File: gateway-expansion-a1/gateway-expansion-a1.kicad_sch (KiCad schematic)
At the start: 3 parts, among them J1 Ruuvi Connector, J2 Ruuvi Connector, J3 Ruuvi Connector

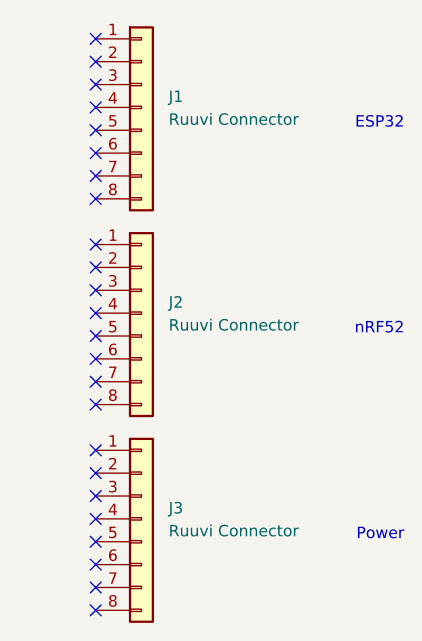
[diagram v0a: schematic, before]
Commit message: Add copper zones and export gerbers
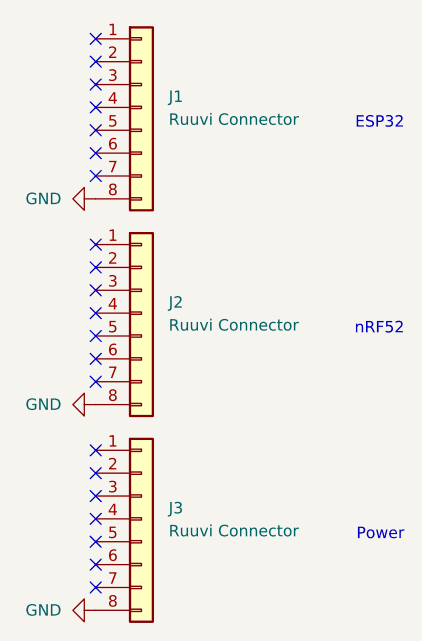
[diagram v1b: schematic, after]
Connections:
- net GND: now reaches J2.8 (Pin_8)
- net GND: now also J1.8 (Pin_8), J3.8 (Pin_8)
- no-connect marks 24 -> 21
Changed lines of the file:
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@@
     (rev "A1")
   )
+  (no_connect (at 124.46 99.06))
+  (no_connect (at 124.46 109.22))
+  (no_connect (at 124.46 129.54))
+  (no_connect (at 124.46 76.2))
+  (no_connect (at 124.46 86.36))
+  (no_connect (at 124.46 83.82))
+  (no_connect (at 124.46 104.14))
+  (no_connect (at 124.46 106.68))
   (no_connect (at 124.46 119.38))
+  (no_connect (at 124.46 127))
+  (no_connect (at 124.46 121.92))
+  (no_connect (at 124.46 81.28))
+  (no_connect (at 124.46 78.74))
+  (no_connect (at 124.46 73.66))
+  (no_connect (at 124.46 132.08))
+  (no_connect (at 124.46 93.98))
   (no_connect (at 124.46 124.46))
-  (no_connect (at 124.46 86.36))
-  (no_connect (at 124.46 81.28))
-  (no_connect (at 124.46 76.2))
-  (no_connect (at 124.46 111.76))
-  (no_connect (at 124.46 104.14))
-  (no_connect (at 124.46 88.9))
-  (no_connect (at 124.46 129.54))
+  (no_connect (at 124.46 116.84))
+  (no_connect (at 124.46 71.12))
+  (no_connect (at 124.46 101.6))
   (no_connect (at 124.46 96.52))
-  (no_connect (at 124.46 116.84))
-  (no_connect (at 124.46 83.82))
-  (no_connect (at 124.46 121.92))
-  (no_connect (at 124.46 109.22))
-  (no_connect (at 124.46 71.12))
-  (no_connect (at 124.46 134.62))
-  (no_connect (at 124.46 93.98))
-  (no_connect (at 124.46 73.66))
-  (no_connect (at 124.46 127))
-  (no_connect (at 124.46 132.08))
-  (no_connect (at 124.46 99.06))
-  (no_connect (at 124.46 101.6))
-  (no_connect (at 124.46 78.74))
-  (no_connect (at 124.46 106.68))
   (text "ESP32" (at 158.75 81.28 180)
     (effects (font (size 1.27 1.27)) (justify right bottom))
@@
   (text "Power" (at 158.75 127 180)
     (effects (font (size 1.27 1.27)) (justify right bottom))
+  )
+  (symbol (lib_id "power:GND") (at 124.46 88.9 270) (unit 1)
+    (in_bom yes) (on_board yes)
+    (property "Reference" "#PWR?" (id 0) (at 118.11 88.9 0)
+      (effects (font (size 1.27 1.27)) hide)
+    )
+    (property "Value" "GND" (id 1) (at 120.65 88.9 90)
+      (effects (font (size 1.27 1.27)) (justify right))
+    )
+    (property "Footprint" "" (id 2) (at 124.46 88.9 0)
+      (effects (font (size 1.27 1.27)) hide)
+    )
+    (property "Datasheet" "" (id 3) (at 124.46 88.9 0)
+      (effects (font (size 1.27 1.27)) hide)
+    )
+  )
+  (symbol (lib_id "power:GND") (at 124.46 111.76 270) (unit 1)
+    (in_bom yes) (on_board yes)
+    (property "Reference" "#PWR?" (id 0) (at 118.11 111.76 0)
+      (effects (font (size 1.27 1.27)) hide)
+    )
+    (property "Value" "GND" (id 1) (at 120.65 111.76 90)
+      (effects (font (size 1.27 1.27)) (justify right))
+    )
+    (property "Footprint" "" (id 2) (at 124.46 111.76 0)
+      (effects (font (size 1.27 1.27)) hide)
+    )
+    (property "Datasheet" "" (id 3) (at 124.46 111.76 0)
+      (effects (font (size 1.27 1.27)) hide)
+    )
+  )
+  (symbol (lib_id "power:GND") (at 124.46 134.62 270) (unit 1)
+    (in_bom yes) (on_board yes)
+    (property "Reference" "#PWR?" (id 0) (at 118.11 134.62 0)
+      (effects (font (size 1.27 1.27)) hide)
+    )
+    (property "Value" "GND" (id 1) (at 120.65 134.62 90)
+      (effects (font (size 1.27 1.27)) (justify right))
+    )
+    (property "Footprint" "" (id 2) (at 124.46 134.62 0)
+      (effects (font (size 1.27 1.27)) hide)
+    )
+    (property "Datasheet" "" (id 3) (at 124.46 134.62 0)
+      (effects (font (size 1.27 1.27)) hide)
+    )
   )
   (symbol (lib_id "Connector_Generic:Conn_01x08") (at 129.54 78.74 0) (unit 1)
@@
   )
   (symbol_instances
+    (path "/4a92fe13-5350-425a-861a-e4dc7fa46a5c"
+      (reference "#PWR?") (unit 1)
+    )
+    (path "/83849df6-5397-4bb1-bacb-3bd39df4c471"
+      (reference "#PWR?") (unit 1)
+    )
+    (path "/f540fc13-343d-4809-87cb-647e5b8603bd"
+      (reference "#PWR?") (unit 1)
+    )
     (path "/f6dbefdc-ad51-4096-b418-e468e21dd444"
       (reference "J1") (unit 1)
